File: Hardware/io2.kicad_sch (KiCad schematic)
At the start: 15 parts, among them U1 H616

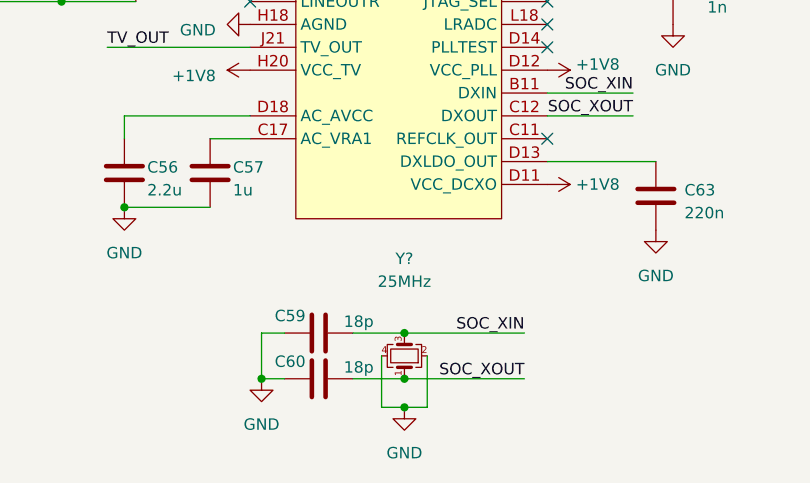
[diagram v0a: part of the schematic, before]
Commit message: fixed crystal resonator value
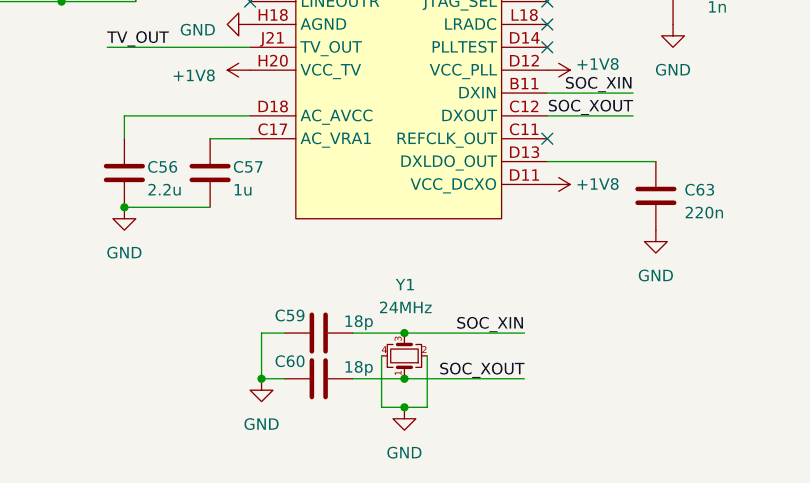
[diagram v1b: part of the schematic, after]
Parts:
- Y1: renamed from Y?; value 25MHz -> 24MHz
